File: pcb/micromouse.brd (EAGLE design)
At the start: 71.1 x 48.3 mm, 29 parts, among them J1 ENCODER_POLOLU, J2 ENCODER_POLOLU, Q1 PFET, U1 DRV8833PWP, U2 LD1117

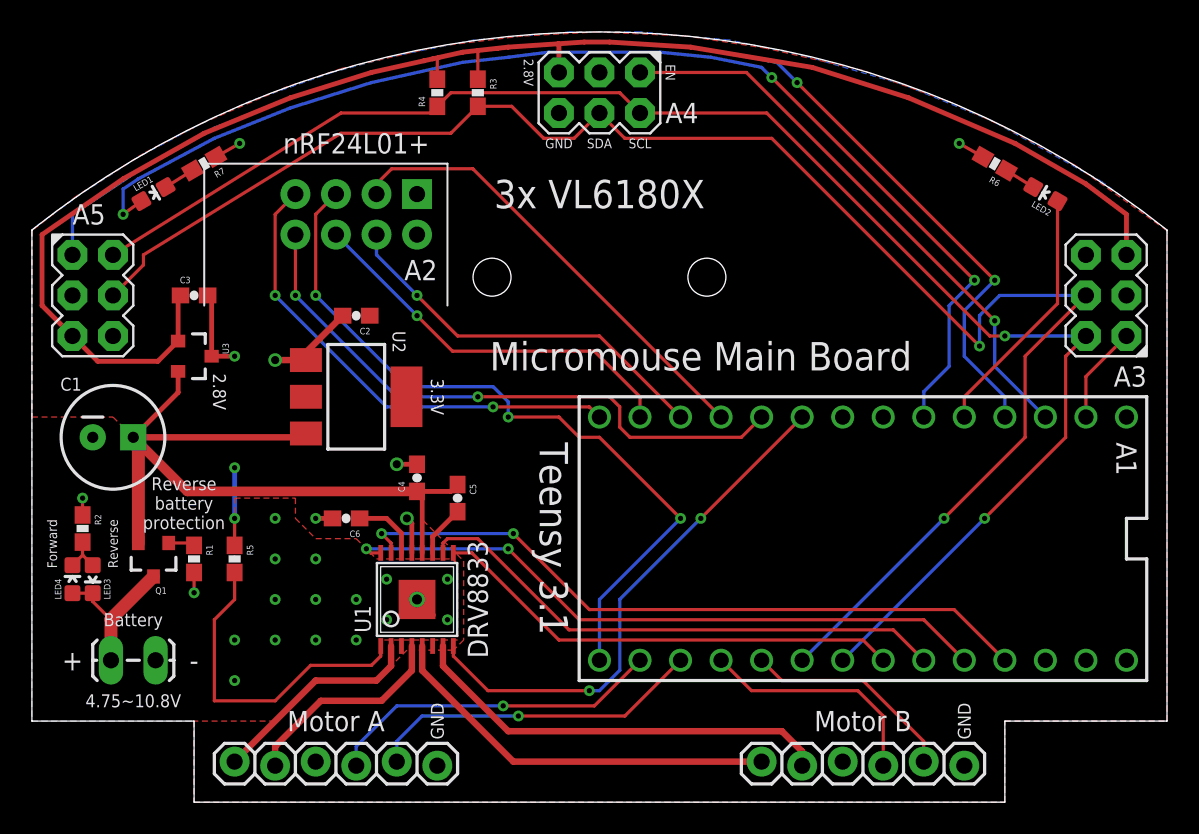
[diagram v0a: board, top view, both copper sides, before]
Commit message: Added buzzer
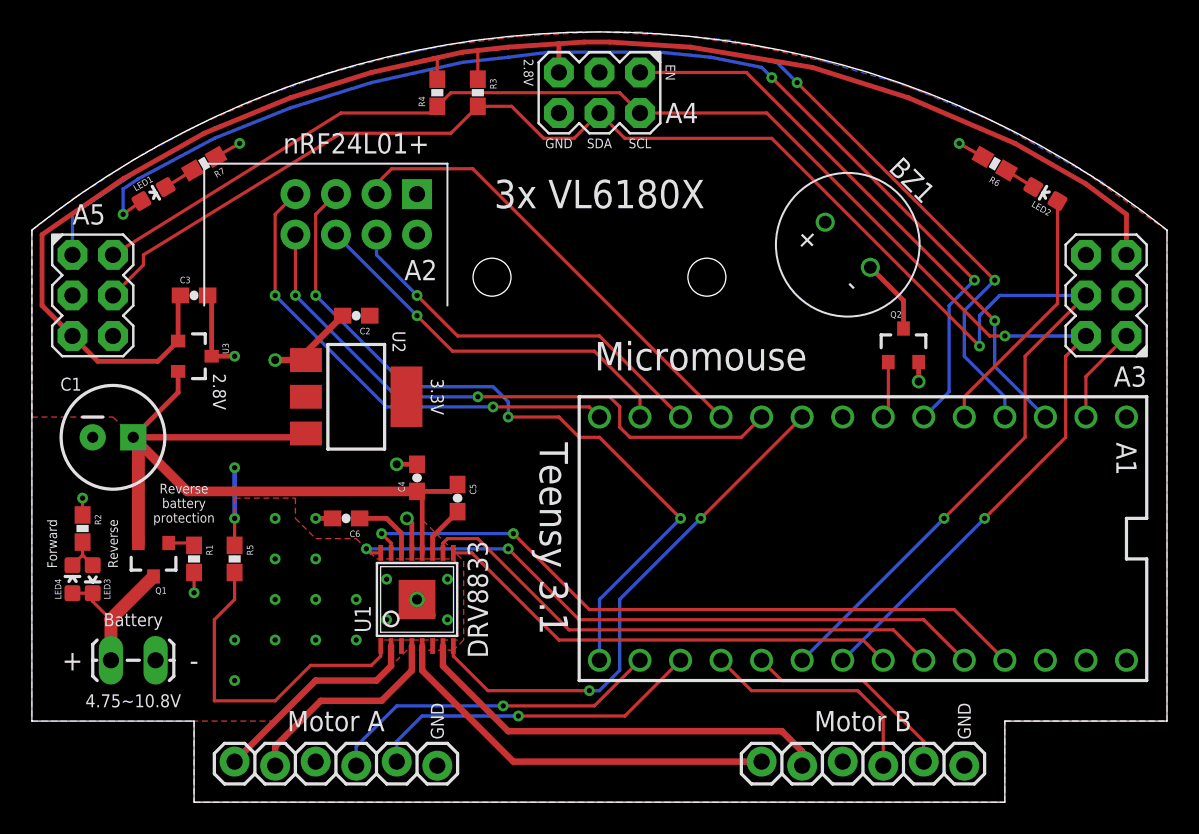
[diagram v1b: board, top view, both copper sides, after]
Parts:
- added BZ1: BUZZER, Custom:BUZZER
- added Q2: (no value), SparkFun-DiscreteSemi:SOT23-3
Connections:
- new net BUZZ: A1.5, Q2.1
- new net N$8: BZ1.-, Q2.3
- net 3.3V: now also BZ1.+
- net GND: now also Q2.2
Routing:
- net N$8: track 0.00 -> 4.70 mm
- net BUZZ: track 0.00 -> 3.58 mm
- net GND: track 24.1 -> 25.4 mm, vias 25 -> 26
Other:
- board text added: "Micromouse"
- board text removed: "Micromouse Main Board"
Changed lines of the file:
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@@
 <circle x="42.291" y="32.893" radius="2.54" width="0" layer="41"/>
 <circle x="28.829" y="32.893" radius="2.54" width="0" layer="42"/>
-<text x="41.91" y="27.94" size="1.778" layer="21" rot="R180" align="center">Micromouse Main Board</text>
+<text x="41.91" y="27.94" size="1.778" layer="21" rot="R180" align="center">Micromouse</text>
 <text x="44.45" y="13.97" size="1.778" layer="22" rot="MR0" align="center">UCSB Robotics Club
 Patrick Clary, 2015</text>
@@
 <text x="58.42" y="5.08" size="0.8128" layer="21" rot="R90" align="center">GND</text>
 <text x="27.94" y="12.7" size="1.27" layer="21" rot="R90" align="center">DRV8833</text>
-<text x="9.525" y="18.7325" size="0.8128" layer="21" align="center">Reverse
+<text x="9.525" y="18.7325" size="0.6096" layer="21" align="center">Reverse
 battery
 protection</text>
@@
 <element name="U3" library="SparkFun-PowerIC" package="SOT23-3" value="" x="10.16" y="27.94" rot="R270"/>
 <element name="C4" library="SparkFun-Capacitors" package="0603-CAP" value="1uF" x="24.13" y="20.32" rot="R90"/>
+<element name="BZ1" library="Custom" package="BUZZER" value="BUZZER" x="51.1175" y="34.925" smashed="yes" rot="R135">
+<attribute name="NAME" x="55.1659125" y="38.9734125" size="1.27" layer="25" rot="R135" align="center"/>
+</element>
+<element name="Q2" library="SparkFun-DiscreteSemi" package="SOT23-3" value="" x="54.61" y="28.575">
+<attribute name="PROD_ID" value="TRANS-08345" x="54.61" y="28.575" size="0.8128" layer="27" display="off"/>
+</element>
 </elements>
 <signals>
@@
 <wire x1="11.53111875" y1="40.43" x2="13.0175" y2="41.275" width="0.2032" layer="1"/>
 <via x="13.0175" y="41.275" extent="1-16" drill="0.3302"/>
+<contactref element="Q2" pad="2"/>
+<wire x1="55.56" y1="27.575" x2="55.56" y2="26.3525" width="0.3048" layer="1"/>
+<via x="55.56" y="26.3525" extent="1-16" drill="0.508"/>
 </signal>
 <signal name="VDD">
@@
 <wire x1="12.7" y1="17.78" x2="12.7" y2="20.955" width="0.3048" layer="16"/>
 <via x="12.7" y="20.955" extent="1-16" drill="0.3302"/>
+<contactref element="BZ1" pad="+"/>
 </signal>
 <signal name="2.8V">
@@
 <wire x1="29.845" y1="46.6725" x2="32.385" y2="46.99" width="0.2032" layer="16"/>
 <wire x1="32.385" y1="46.99" x2="39.37" y2="46.99" width="0.2032" layer="16"/>
-<wire x1="55.88" y1="24.13" x2="55.88" y2="25.7175" width="0.2032" layer="16"/>
-<wire x1="55.88" y1="25.7175" x2="57.4675" y2="27.305" width="0.2032" layer="16"/>
-<wire x1="57.4675" y1="27.305" x2="57.4675" y2="31.115" width="0.2032" layer="16"/>
+<wire x1="57.4675" y1="25.7175" x2="57.4675" y2="31.115" width="0.2032" layer="16"/>
 <wire x1="57.4675" y1="31.115" x2="59.055" y2="32.7025" width="0.2032" layer="16"/>
 <via x="59.055" y="32.7025" extent="1-16" drill="0.3302"/>
@@
 <wire x1="45.72" y1="46.0375" x2="42.545" y2="46.6725" width="0.2032" layer="16"/>
 <wire x1="42.545" y1="46.6725" x2="39.37" y2="46.99" width="0.2032" layer="16"/>
+<wire x1="55.88" y1="24.13" x2="57.4675" y2="25.7175" width="0.2032" layer="16"/>
 </signal>
 <signal name="N$5">
@@
 <wire x1="48.26" y1="3.175" x2="48.26" y2="2.286" width="0.4064" layer="1"/>
 </signal>
+<signal name="N$8">
+<contactref element="BZ1" pad="-"/>
+<contactref element="Q2" pad="3"/>
+<wire x1="54.61" y1="29.675" x2="54.61" y2="31.432496875" width="0.3048" layer="1"/>
+<wire x1="54.61" y1="31.432496875" x2="52.5317125" y2="33.510784375" width="0.3048" layer="1"/>
+</signal>
+<signal name="BUZZ">
+<contactref element="A1" pad="5"/>
+<contactref element="Q2" pad="1"/>
+<wire x1="53.66" y1="27.575" x2="53.66" y2="24.45" width="0.2032" layer="1"/>
+<wire x1="53.66" y1="24.45" x2="53.34" y2="24.13" width="0.2032" layer="1"/>
+</signal>
 </signals>

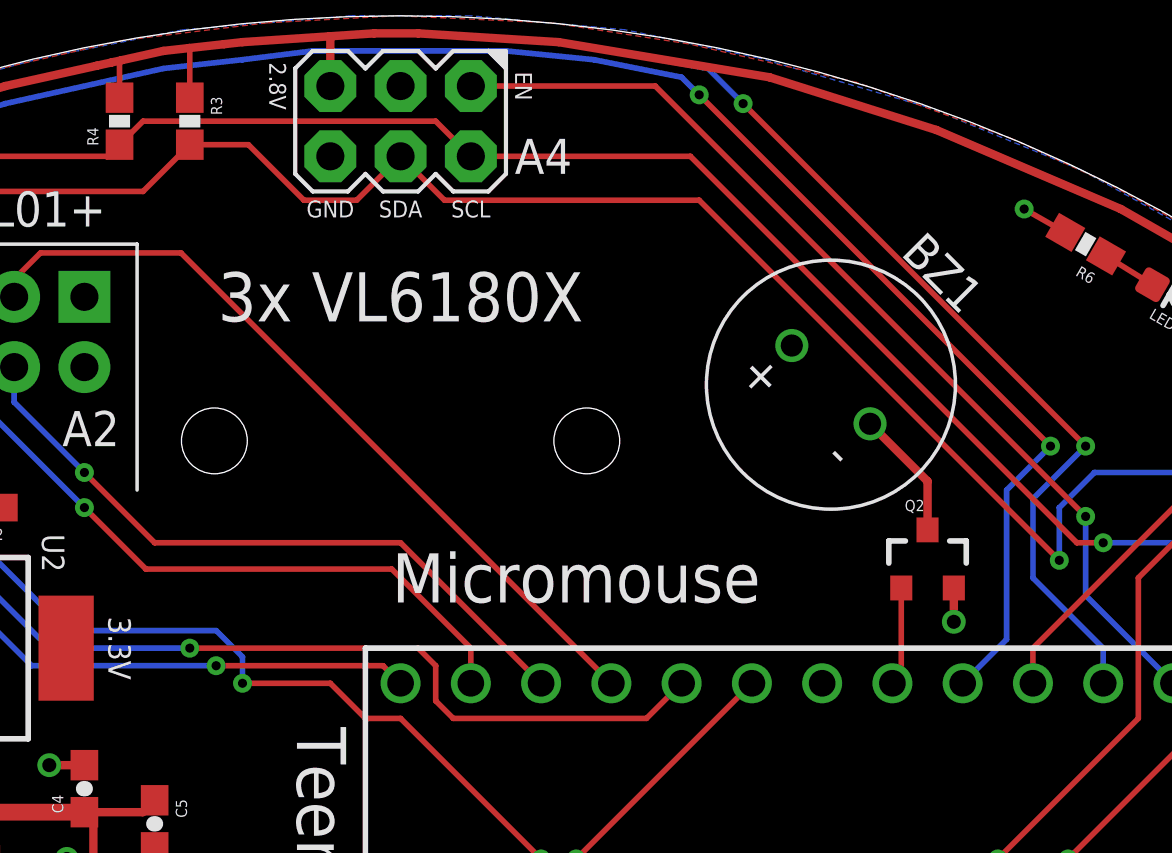
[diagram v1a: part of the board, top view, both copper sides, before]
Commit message: Improved buzzer drive circuitry
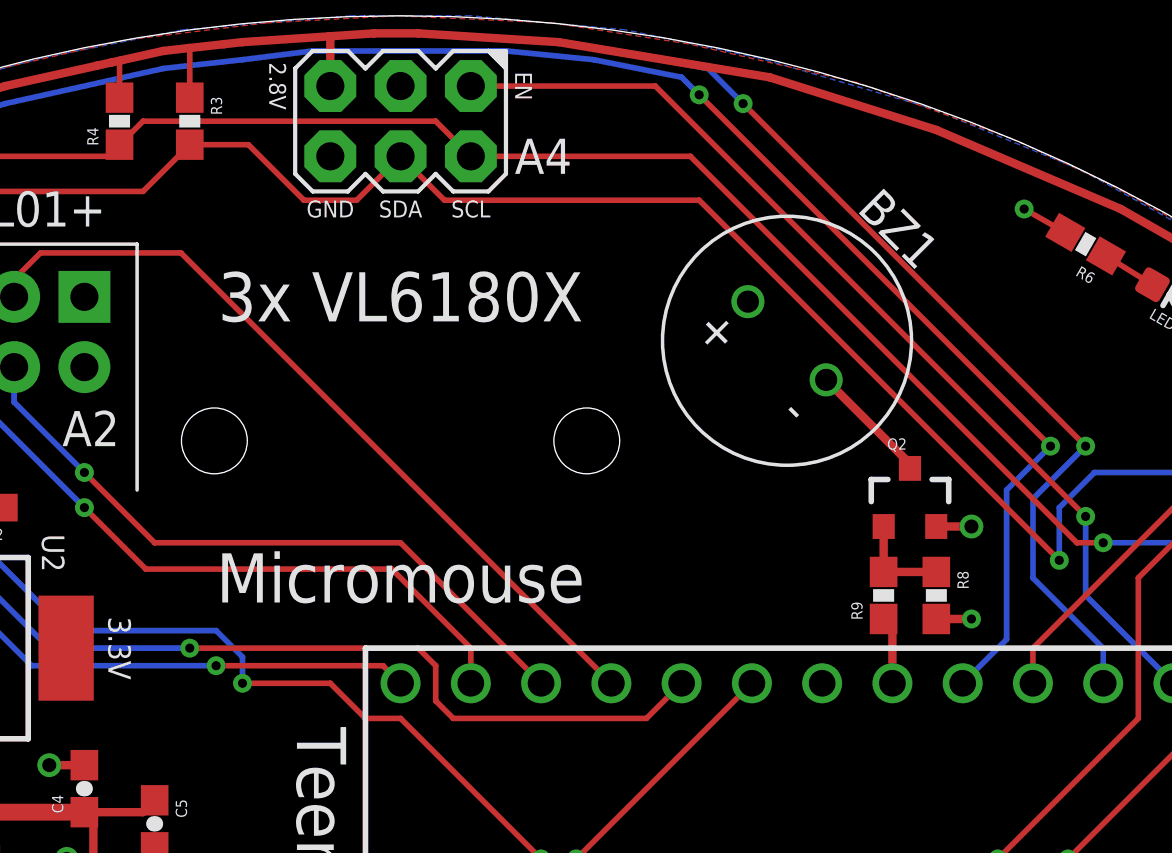
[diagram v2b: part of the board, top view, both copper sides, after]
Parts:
- added R8: 100K, SparkFun-Resistors:0603-RES
- added R9: 132, SparkFun-Resistors:0603-RES
- moved Q2 2.31 mm to (54.0, 30.8)
- moved BZ1 2.25 mm to (49.5, 36.5)
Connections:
- new net N$15: Q2.1, R8.1, R9.2
- net BUZZ: now also R9.1; no longer Q2.1
- net GND: now also R8.2
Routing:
- net N$15: track 0.00 -> 3.55 mm
- net GND: track 25.4 -> 26.7 mm, vias 26 -> 27
- net BUZZ: track 3.58 -> 2.46 mm
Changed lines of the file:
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@@
 <circle x="42.291" y="32.893" radius="2.54" width="0" layer="41"/>
 <circle x="28.829" y="32.893" radius="2.54" width="0" layer="42"/>
-<text x="41.91" y="27.94" size="1.778" layer="21" rot="R180" align="center">Micromouse</text>
+<text x="35.56" y="27.94" size="1.778" layer="21" rot="R180" align="center">Micromouse</text>
 <text x="44.45" y="13.97" size="1.778" layer="22" rot="MR0" align="center">UCSB Robotics Club
 Patrick Clary, 2015</text>
@@
 <element name="U3" library="SparkFun-PowerIC" package="SOT23-3" value="" x="10.16" y="27.94" rot="R270"/>
 <element name="C4" library="SparkFun-Capacitors" package="0603-CAP" value="1uF" x="24.13" y="20.32" rot="R90"/>
-<element name="BZ1" library="Custom" package="BUZZER" value="BUZZER" x="51.1175" y="34.925" smashed="yes" rot="R135">
-<attribute name="NAME" x="55.1659125" y="38.9734125" size="1.27" layer="25" rot="R135" align="center"/>
-</element>
-<element name="Q2" library="SparkFun-DiscreteSemi" package="SOT23-3" value="" x="54.61" y="28.575">
-<attribute name="PROD_ID" value="TRANS-08345" x="54.61" y="28.575" size="0.8128" layer="27" display="off"/>
-</element>
+<element name="BZ1" library="Custom" package="BUZZER" value="BUZZER" x="49.53" y="36.5125" smashed="yes" rot="R135">
+<attribute name="NAME" x="53.5784125" y="40.5609125" size="1.27" layer="25" rot="R135" align="center"/>
+</element>
+<element name="Q2" library="SparkFun-DiscreteSemi" package="SOT23-3" value="" x="53.975" y="30.7975">
+<attribute name="PROD_ID" value="TRANS-08345" x="53.975" y="30.7975" size="0.8128" layer="27" display="off"/>
+</element>
+<element name="R8" library="SparkFun-Resistors" package="0603-RES" value="100K" x="54.9275" y="27.305" rot="R270"/>
+<element name="R9" library="SparkFun-Resistors" package="0603-RES" value="132" x="53.0225" y="27.305" rot="R90"/>
 </elements>
 <signals>
@@
 <via x="13.0175" y="41.275" extent="1-16" drill="0.3302"/>
 <contactref element="Q2" pad="2"/>
-<wire x1="55.56" y1="27.575" x2="55.56" y2="26.3525" width="0.3048" layer="1"/>
-<via x="55.56" y="26.3525" extent="1-16" drill="0.508"/>
+<contactref element="R8" pad="2"/>
+<wire x1="54.9275" y1="29.795" x2="54.925" y2="29.7975" width="0.3048" layer="1"/>
+<wire x1="54.925" y1="29.7975" x2="56.1975" y2="29.7975" width="0.3048" layer="1"/>
+<wire x1="54.9275" y1="26.455" x2="56.1975" y2="26.455" width="0.3048" layer="1"/>
+<via x="56.1975" y="29.7975" extent="1-16" drill="0.508"/>
+<via x="56.1975" y="26.455" extent="1-16" drill="0.3302"/>
 </signal>
 <signal name="VDD">
@@
 <contactref element="BZ1" pad="-"/>
 <contactref element="Q2" pad="3"/>
-<wire x1="54.61" y1="29.675" x2="54.61" y2="31.432496875" width="0.3048" layer="1"/>
-<wire x1="54.61" y1="31.432496875" x2="52.5317125" y2="33.510784375" width="0.3048" layer="1"/>
+<wire x1="50.9442125" y1="35.098284375" x2="53.975" y2="32.067496875" width="0.3048" layer="1"/>
+<wire x1="53.975" y1="32.067496875" x2="53.975" y2="31.8975" width="0.3048" layer="1"/>
 </signal>
 <signal name="BUZZ">
 <contactref element="A1" pad="5"/>
+<contactref element="R9" pad="1"/>
+<wire x1="53.34" y1="24.13" x2="53.34" y2="26.1375" width="0.3048" layer="1"/>
+<wire x1="53.34" y1="26.1375" x2="53.0225" y2="26.455" width="0.3048" layer="1"/>
+</signal>
+<signal name="N$15">
 <contactref element="Q2" pad="1"/>
-<wire x1="53.66" y1="27.575" x2="53.66" y2="24.45" width="0.2032" layer="1"/>
-<wire x1="53.66" y1="24.45" x2="53.34" y2="24.13" width="0.2032" layer="1"/>
+<contactref element="R8" pad="1"/>
+<contactref element="R9" pad="2"/>
+<wire x1="53.0225" y1="28.155" x2="53.0225" y2="29.7975" width="0.3048" layer="1"/>
+<wire x1="53.0225" y1="29.7975" x2="53.025" y2="29.7975" width="0.3048" layer="1"/>
+<wire x1="54.9275" y1="28.155" x2="53.0225" y2="28.155" width="0.3048" layer="1"/>
 </signal>
 </signals>
